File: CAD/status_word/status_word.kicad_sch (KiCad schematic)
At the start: 23 parts, among them J1 Conn_SW, U1 74HC377, U2 74HC109, U3 74HC157, U4 74HC157, U5 74HC245, U6 74HC02

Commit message: add Status Word PCB, not finished
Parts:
- removed U1: 74HC377, symbol 8bit_computer:74HC377
- added C6: 100nF, Capacitor_SMD:C_0805_2012Metric, symbol Device:C
- added D10: STI, LED_SMD:LED_0805_2012Metric, symbol Device:LED
- added D6: SW_IN, LED_SMD:LED_0805_2012Metric, symbol Device:LED
- added D7: SW_OUT, LED_SMD:LED_0805_2012Metric, symbol Device:LED
- added D8: L_FLAGS, LED_SMD:LED_0805_2012Metric, symbol Device:LED
- added D9: CLI, LED_SMD:LED_0805_2012Metric, symbol Device:LED
- added R10, R6, R7, R8, R9: 1k, Resistor_SMD:R_0805_2012Metric, symbol Device:R
- added U1: AFLAGS, Package_SO:SO-16_3.9x9.9mm_P1.27mm, symbol 8bit_computer:74HC161
- added unit 3 of U2
- added unit 1 of U2
- C1, C2, C3, C4, C5: footprint (none) -> Capacitor_SMD:C_0805_2012Metric
- C7: renamed from C6; footprint (none) -> Capacitor_SMD:C_0805_2012Metric
- D1: value CF -> ZF; footprint (none) -> LED_SMD:LED_0805_2012Metric
- D2: value ZF -> CF; footprint (none) -> LED_SMD:LED_0805_2012Metric
- D3, D4, D5: footprint (none) -> LED_SMD:LED_0805_2012Metric
- J1: footprint Connector_PinSocket_2.54mm:PinSocket_2x13_P2.54mm_Horizontal -> Connector_PinHeader_2.54mm:PinHeader_2x13_P2.54mm_Horizontal
- R1, R2, R3, R4, R5: footprint (none) -> Resistor_SMD:R_0805_2012Metric
- U2: value 74HC109 -> IMASK; footprint (none) -> Package_SO:SO-16_3.9x9.9mm_P1.27mm
- U3: value 74HC157 -> MUX1; footprint (none) -> Package_SO:SO-16_3.9x9.9mm_P1.27mm
- U4: value 74HC157 -> MUX2; footprint (none) -> Package_SO:SO-16_3.9x9.9mm_P1.27mm
- U5: value 74HC245 -> BUFFER; footprint (none) -> Package_SO:SO-20_5.3x12.6mm_P1.27mm
- U6: footprint (none) -> Package_SO:SO-14_3.9x8.65mm_P1.27mm
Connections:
- net +5V: now also C6.1, R7.1, U1.16 (VCC), U2.16 (VCC), U2.5 (~{S}); no longer U2.16 (VCC), U2.5 (~{S})
- net GND: now also R1.2, R2.2, R3.2, R4.2, R5.2, C6.2, D10.1 (K), D6.1 (K), D8.1 (K), D9.1 (K), U1.10 (CET), U1.7 (CEP), U1.8 (GND), U2.8 (GND); no longer D1.1 (K), D2.1 (K), D3.1 (K), D4.1 (K), D5.1 (K), U2.8 (GND)
- net aflags_in: now also R8.1
- net cli: now also R9.1
- net clk: now also U1.2 (CP), U2.4 (C); no longer U2.4 (C)
- net mux0: now also U1.3 (D0)
- net mux1: now also U1.4 (D1)
- net mux2: now also U1.5 (D2)
- net mux3: now also U1.6 (D3)
- net sti: now also R10.1
- net sw.cf: now also D2.2 (A), U1.13 (Q1); no longer R2.1
- net sw.im: now also D5.2 (A), U2.6 (Q); no longer R5.1, U2.6 (Q)
- net sw.nf: now also D3.2 (A), U1.12 (Q2); no longer R3.1
- net sw.vf: now also D4.2 (A), U1.11 (Q3); no longer R4.1
- net sw.zf: now also D1.2 (A), U1.14 (Q0); no longer R1.1
- net sw_in: now also R6.1
- net ~{sw_out}: now also D7.1 (K)
- net at U6.1: now also U1.9 (~{PE})
- net at U4.4 (Za): now also U2.2 (J); no longer U2.2 (J)
- net at U4.7 (Zb): now also U2.3 (~{K}); no longer U2.3 (~{K})
- net rst renamed ~{rst}
- net ~{rst}: now also U1.1 (~{MR}), U2.1 (~{R}); no longer U2.1 (~{R})
- new net: D9.2 (A), R9.2
- new net: D7.2 (A), R7.2
- new net: D8.2 (A), R8.2
- new net: D5.1 (K), R5.1
- new net: D6.2 (A), R6.2
- new net: D3.1 (K), R3.1
- new net: D2.1 (K), R2.1
- new net: D1.1 (K), R1.1
- new net: D10.2 (A), R10.2
- new net: D4.1 (K), R4.1
- no-connect marks 11 -> 8
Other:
- moved on the sheet: C1, C2, C3, C4, C5, D1, D2, D3, D4, D5, R1, R2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

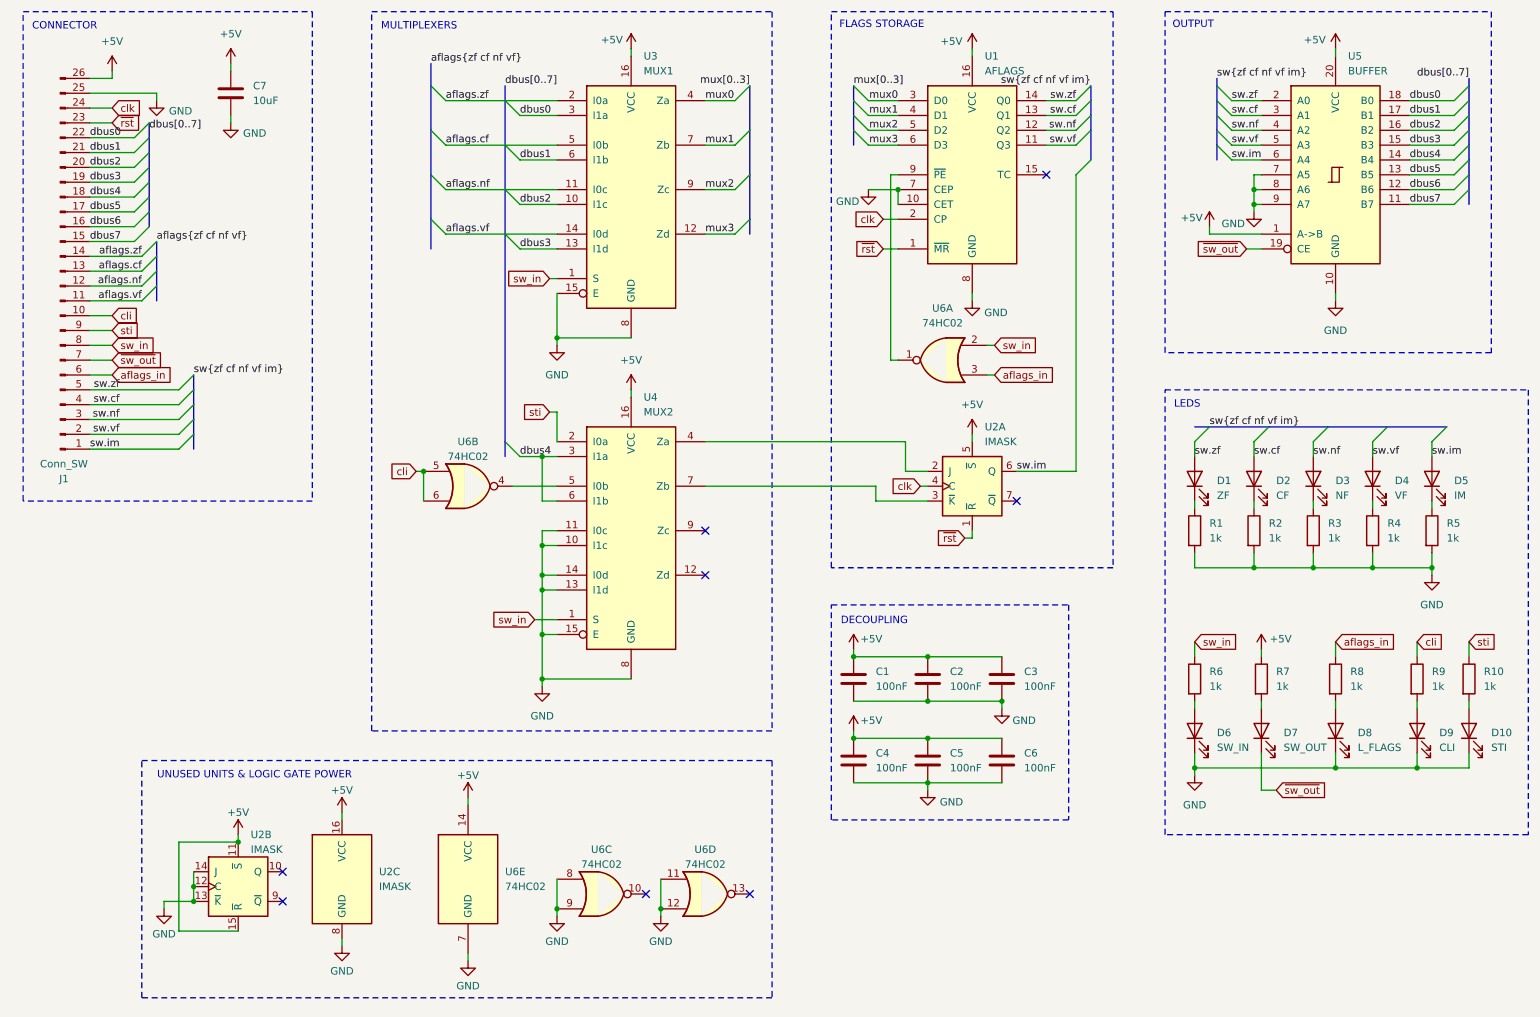
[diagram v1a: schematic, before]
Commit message: add mounting holes, pull-up, test points in SW
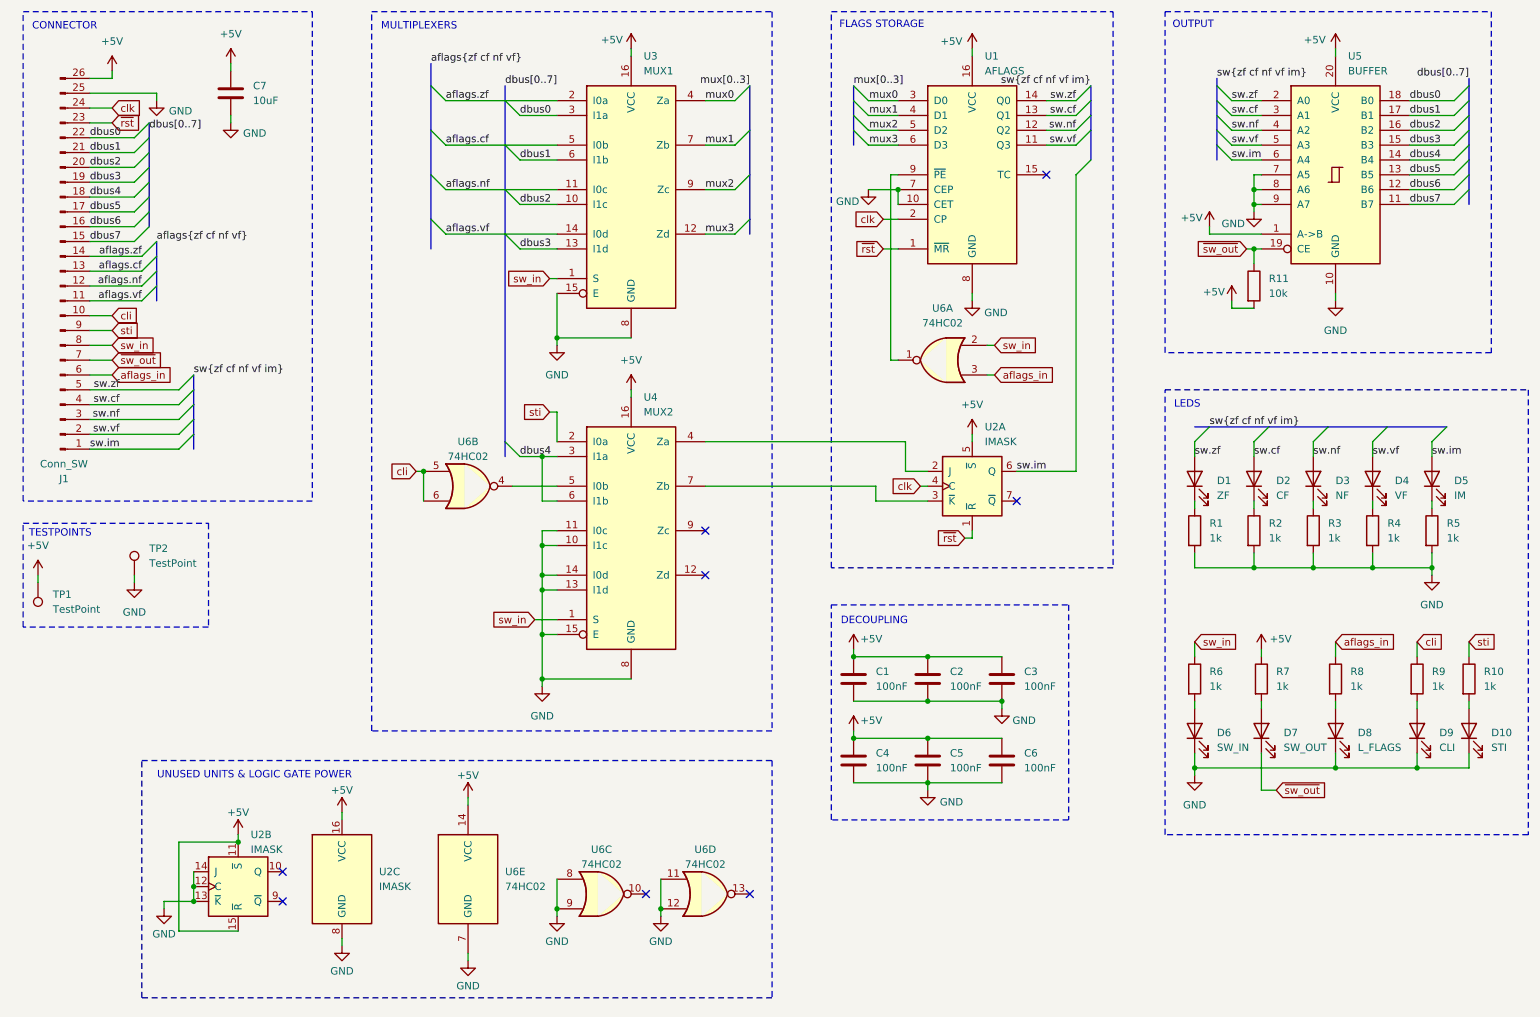
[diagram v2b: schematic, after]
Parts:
- added R11: 10k, Resistor_SMD:R_0805_2012Metric, symbol Device:R
- added TP1, TP2: TestPoint, TestPoint:TestPoint_THTPad_D1.0mm_Drill0.5mm, symbol Connector:TestPoint
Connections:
- net +5V: now also R11.2, TP1.1
- net GND: now also TP2.1
- net ~{sw_out}: now also R11.1
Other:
- note added: "TESTPOINTS"

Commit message: update silkscreen qr code, license, add images
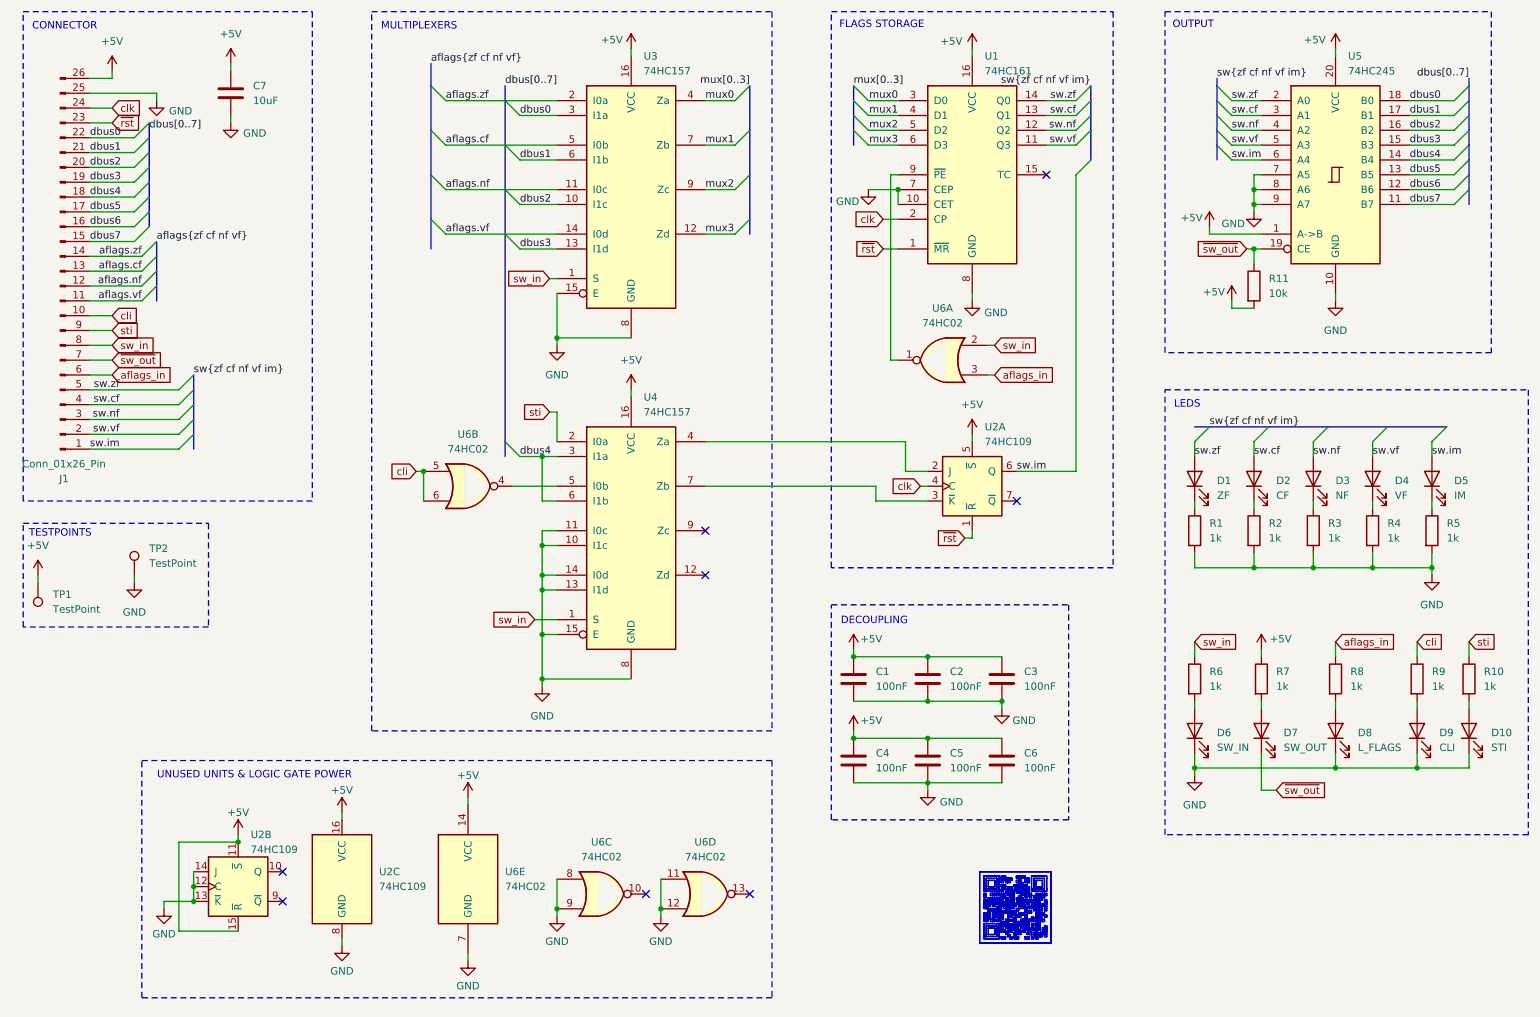
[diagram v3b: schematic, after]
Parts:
- J1: value Conn_SW -> Conn_01x26_Pin
- U1: value AFLAGS -> 74HC161; Details (none) -> https://www.lcsc.com/product-detail/C6824.html; LCSC (none) -> C6824
- U2: value IMASK -> 74HC109; Details (none) -> https://www.lcsc.com/product-detail/C2860677.html; LCSC (none) -> C2860677
- U3: value MUX1 -> 74HC157; Details (none) -> https://www.lcsc.com/product-detail/C6823.html; LCSC (none) -> C6823
- U4: value MUX2 -> 74HC157; Details (none) -> https://www.lcsc.com/product-detail/C6823.html; LCSC (none) -> C6823
- U5: value BUFFER -> 74HC245; symbol 74xx:74HC245 -> 8bit_computer:74HC245; Details (none) -> https://www.lcsc.com/product-detail/C88578.html; LCSC (none) -> C88578
- U6: symbol 74xx:74HC02 -> 8bit_computer:74HC02; Details (none) -> https://www.lcsc.com/product-detail/C253895.html; LCSC (none) -> C253895

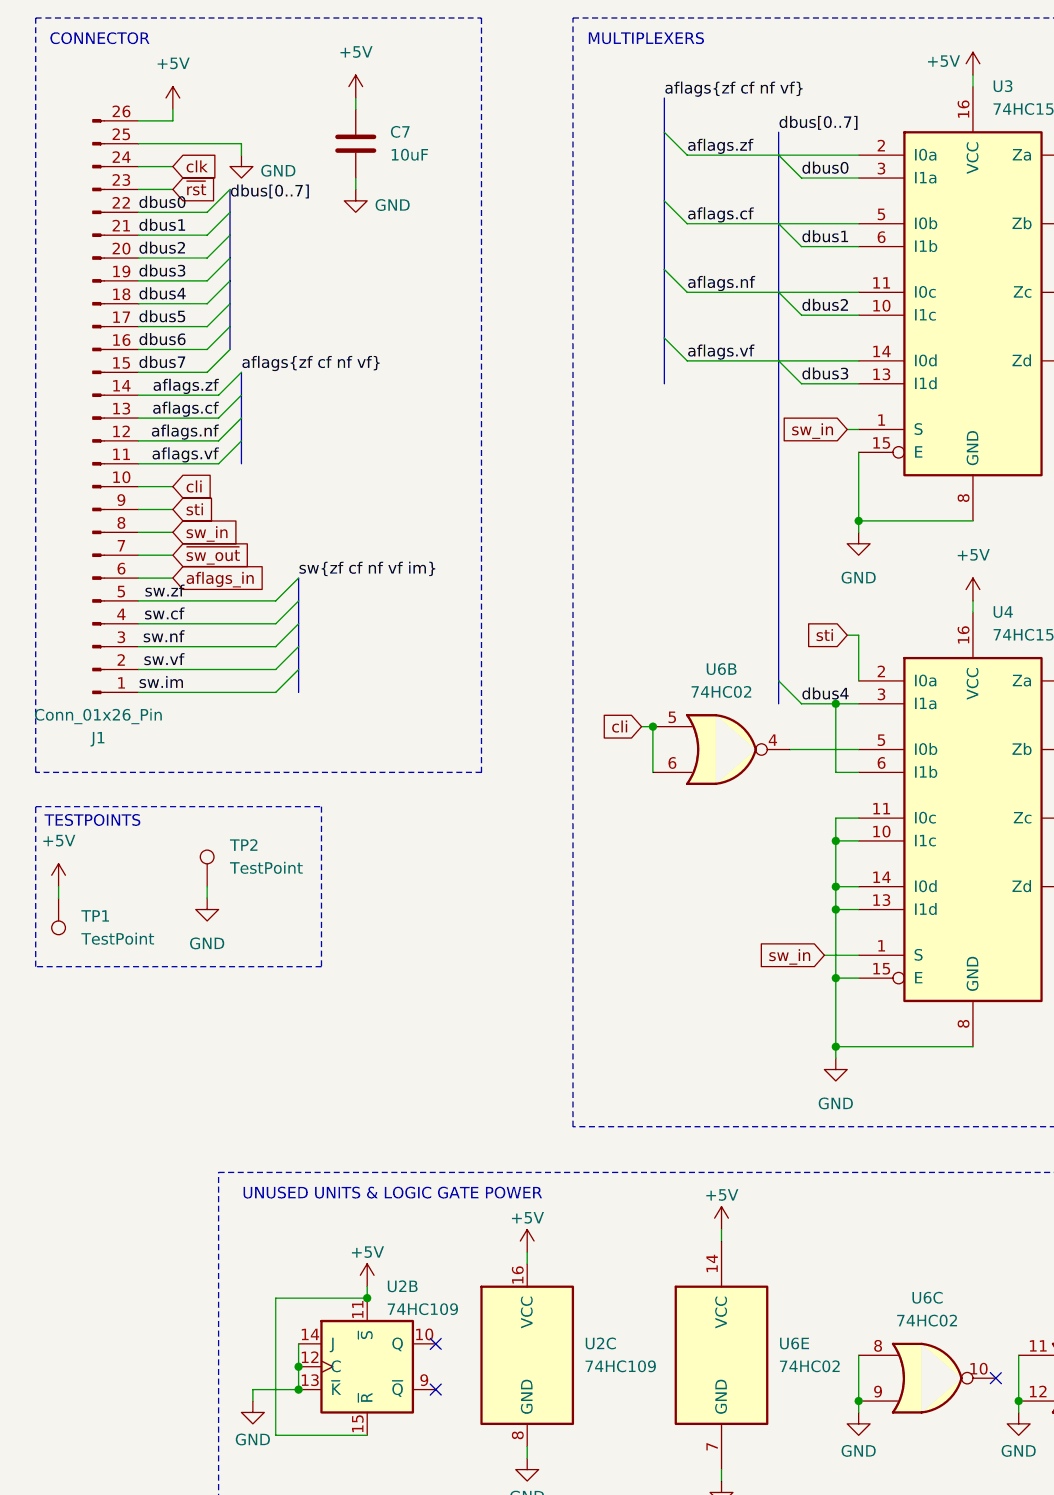
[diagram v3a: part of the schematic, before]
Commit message: layout changes, adding mounting holes, modifying tooling holes and adding fiducials
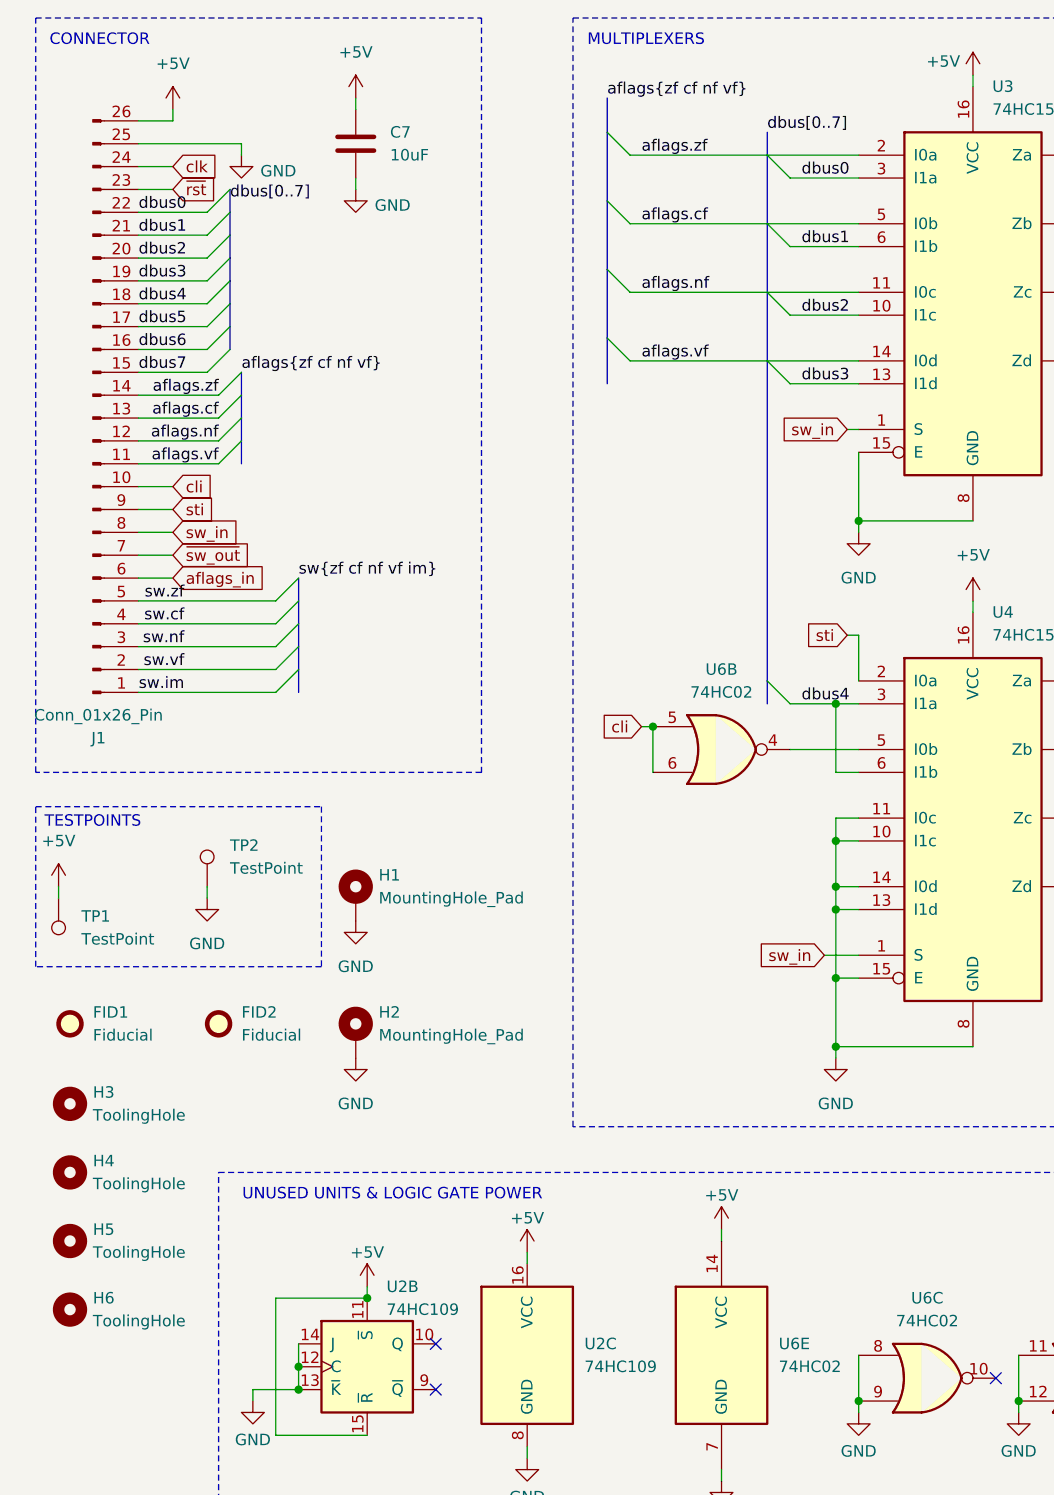
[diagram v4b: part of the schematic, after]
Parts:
- added FID1, FID2: Fiducial, Fiducial:Fiducial_0.5mm_Mask1mm, symbol Mechanical:Fiducial
- added H1, H2: MountingHole_Pad, MountingHole:MountingHole_2.5mm_Pad_Via, symbol Mechanical:MountingHole_Pad
- added H3, H4, H5, H6: ToolingHole, MountingHole:ToolingHole_1.152mm, symbol Mechanical:MountingHole
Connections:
- net GND: now also H1.1, H2.1

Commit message: change buffer footprint in SW
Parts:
- U5: footprint Package_SO:SO-20_5.3x12.6mm_P1.27mm -> Package_SO:SOIC-20W_7.5x12.8mm_P1.27mm; Details https://www.lcsc.com/product-detail/C88578.html -> https://jlcpcb.com/partdetail/Nexperia-74HC245D653/C5625; LCSC C88578 -> C5625
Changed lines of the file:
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@@
 			)
 		)
-		(property "Footprint" "Package_SO:SO-20_5.3x12.6mm_P1.27mm"
+		(property "Footprint" "Package_SO:SOIC-20W_7.5x12.8mm_P1.27mm"
 			(at 240.03 48.26 0)
 			(effects
@@
 			)
 		)
-		(property "Datasheet" "https://www.lcsc.com/datasheet/C88578.pdf"
+		(property "Datasheet" "https://jlcpcb.com/api/file/downloadByFileSystemAccessId/8579708648597213184"
 			(at 240.03 48.26 0)
 			(effects
@@
 			)
 		)
-		(property "Details" "https://www.lcsc.com/product-detail/C88578.html"
+		(property "Details" "https://jlcpcb.com/partdetail/Nexperia-74HC245D653/C5625"
 			(at 240.03 48.26 0)
 			(effects
@@
 			)
 		)
-		(property "LCSC" "C88578"
+		(property "LCSC" "C5625"
 			(at 240.03 48.26 0)
 			(effects
